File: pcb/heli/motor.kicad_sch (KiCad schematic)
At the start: 6 parts

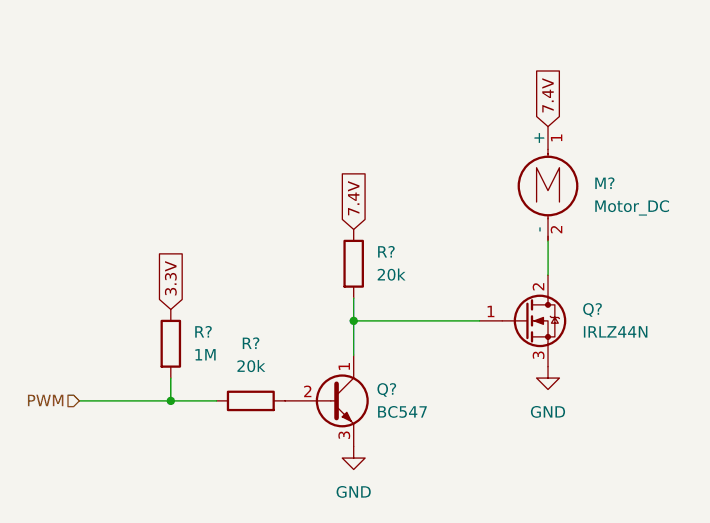
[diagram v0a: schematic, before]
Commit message: 
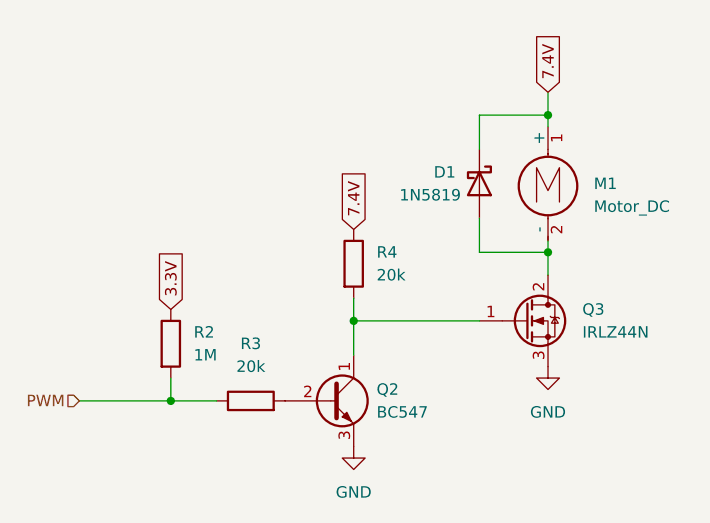
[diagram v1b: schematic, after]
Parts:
- added D1: 1N5819, Diode_THT:D_DO-41_SOD81_P10.16mm_Horizontal, symbol Diode:1N5819
- gave numbers to parts that had none: 6
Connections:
- net 7.4V: now also D1.1 (K)
- net at M1.2 (-), Q3.2 (D): now also D1.2 (A)
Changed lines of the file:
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@@
   (junction (at 54.61 59.69) (diameter 0) (color 0 0 0 0)
   )
+  (junction (at 76.2 36.83) (diameter 0) (color 0 0 0 0)
+  )
+  (junction (at 76.2 52.07) (diameter 0) (color 0 0 0 0)
+  )
   (junction (at 34.29 68.58) (diameter 0) (color 0 0 0 0)
   )
+  (wire (pts (xy 76.2 52.07) (xy 76.2 54.61))
+    (stroke (width 0) (type default) (color 0 0 0 0))
+  )
+  (wire (pts (xy 68.58 36.83) (xy 76.2 36.83))
+    (stroke (width 0) (type default) (color 0 0 0 0))
+  )
+  (wire (pts (xy 68.58 52.07) (xy 76.2 52.07))
+    (stroke (width 0) (type default) (color 0 0 0 0))
+  )
   (wire (pts (xy 54.61 59.69) (xy 54.61 57.15))
     (stroke (width 0) (type default) (color 0 0 0 0))
   )
-  (wire (pts (xy 76.2 50.8) (xy 76.2 54.61))
+  (wire (pts (xy 76.2 50.8) (xy 76.2 52.07))
+    (stroke (width 0) (type default) (color 0 0 0 0))
+  )
+  (wire (pts (xy 68.58 40.64) (xy 68.58 36.83))
+    (stroke (width 0) (type default) (color 0 0 0 0))
+  )
+  (wire (pts (xy 76.2 36.83) (xy 76.2 38.1))
     (stroke (width 0) (type default) (color 0 0 0 0))
   )
@@
   )
   (wire (pts (xy 34.29 68.58) (xy 39.37 68.58))
+    (stroke (width 0) (type default) (color 0 0 0 0))
+  )
+  (wire (pts (xy 76.2 34.29) (xy 76.2 36.83))
+    (stroke (width 0) (type default) (color 0 0 0 0))
+  )
+  (wire (pts (xy 68.58 48.26) (xy 68.58 52.07))
     (stroke (width 0) (type default) (color 0 0 0 0))
   )
@@
     )
   )
-  (global_label "7.4V" (shape input) (at 76.2 38.1 90) (fields_autoplaced)
+  (global_label "7.4V" (shape input) (at 76.2 34.29 90) (fields_autoplaced)
     (effects (font (size 1.27 1.27)) (justify left))
-    (property "Intersheet References" "${INTERSHEET_REFS}" (id 0) (at 76.1206 31.5745 90)
+    (property "Intersheet References" "${INTERSHEET_REFS}" (id 0) (at 76.1206 27.7645 90)
       (effects (font (size 1.27 1.27)) (justify left) hide)
     )
@@
   (symbol (lib_id "power:GND") (at 54.61 73.66 0) (unit 1)
     (in_bom yes) (on_board yes) (fields_autoplaced)
-    (property "Reference" "#PWR?" (id 0) (at 54.61 80.01 0)
+    (property "Reference" "#PWR0115" (id 0) (at 54.61 80.01 0)
       (effects (font (size 1.27 1.27)) hide)
     )
@@
   (symbol (lib_id "Device:R") (at 34.29 62.23 0) (unit 1)
     (in_bom yes) (on_board yes) (fields_autoplaced)
-    (property "Reference" "R?" (id 0) (at 36.83 60.9599 0)
+    (property "Reference" "R2" (id 0) (at 36.83 60.9599 0)
       (effects (font (size 1.27 1.27)) (justify left))
     )
@@
     (pin "2")
   )
+  (symbol (lib_id "Diode:1N5819") (at 68.58 44.45 270) (unit 1)
+    (in_bom yes) (on_board yes)
+    (property "Reference" "D1" (id 0) (at 63.5 43.18 90)
+      (effects (font (size 1.27 1.27)) (justify left))
+    )
+    (property "Value" "1N5819" (id 1) (at 59.69 45.72 90)
+      (effects (font (size 1.27 1.27)) (justify left))
+    )
+    (property "Footprint" "Diode_THT:D_DO-41_SOD81_P10.16mm_Horizontal" (id 2) (at 64.135 44.45 0)
+      (effects (font (size 1.27 1.27)) hide)
+    )
+    (property "Datasheet" "http://www.vishay.com/docs/88525/1n5817.pdf" (id 3) (at 68.58 44.45 0)
+      (effects (font (size 1.27 1.27)) hide)
+    )
+    (pin "1")
+    (pin "2")
+  )
   (symbol (lib_id "Device:R") (at 43.18 68.58 90) (unit 1)
     (in_bom yes) (on_board yes) (fields_autoplaced)
-    (property "Reference" "R?" (id 0) (at 43.18 62.23 90))
+    (property "Reference" "R3" (id 0) (at 43.18 62.23 90))
     (property "Value" "20k" (id 1) (at 43.18 64.77 90))
     (property "Footprint" "" (id 2) (at 43.18 70.358 90)
@@
   (symbol (lib_id "Transistor_BJT:BC547") (at 52.07 68.58 0) (unit 1)
     (in_bom yes) (on_board yes) (fields_autoplaced)
-    (property "Reference" "Q?" (id 0) (at 57.15 67.3099 0)
+    (property "Reference" "Q2" (id 0) (at 57.15 67.3099 0)
       (effects (font (size 1.27 1.27)) (justify left))
     )
@@
   (symbol (lib_id "power:GND") (at 76.2 64.77 0) (unit 1)
     (in_bom yes) (on_board yes) (fields_autoplaced)
-    (property "Reference" "#PWR?" (id 0) (at 76.2 71.12 0)
+    (property "Reference" "#PWR0114" (id 0) (at 76.2 71.12 0)
       (effects (font (size 1.27 1.27)) hide)
     )
@@
   (symbol (lib_id "Device:R") (at 54.61 53.34 0) (unit 1)
     (in_bom yes) (on_board yes) (fields_autoplaced)
-    (property "Reference" "R?" (id 0) (at 57.15 52.0699 0)
+    (property "Reference" "R4" (id 0) (at 57.15 52.0699 0)
       (effects (font (size 1.27 1.27)) (justify left))
     )
@@
   (symbol (lib_id "Transistor_FET:IRLZ44N") (at 73.66 59.69 0) (unit 1)
     (in_bom yes) (on_board yes) (fields_autoplaced)
-    (property "Reference" "Q?" (id 0) (at 80.01 58.4199 0)
+    (property "Reference" "Q3" (id 0) (at 80.01 58.4199 0)
       (effects (font (size 1.27 1.27)) (justify left))
     )
@@
   (symbol (lib_id "Motor:Motor_DC") (at 76.2 43.18 0) (unit 1)
     (in_bom yes) (on_board yes) (fields_autoplaced)
-    (property "Reference" "M?" (id 0) (at 81.28 44.4499 0)
-      (effects (font (size 1.27 1.27)) (justify left))
-    )
+    (property "Reference" "M1" (id 0) (at 81.28 44.4499 0)
+      (effects (font (size 1.27 1.27)) (justify left))
+    )

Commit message: 
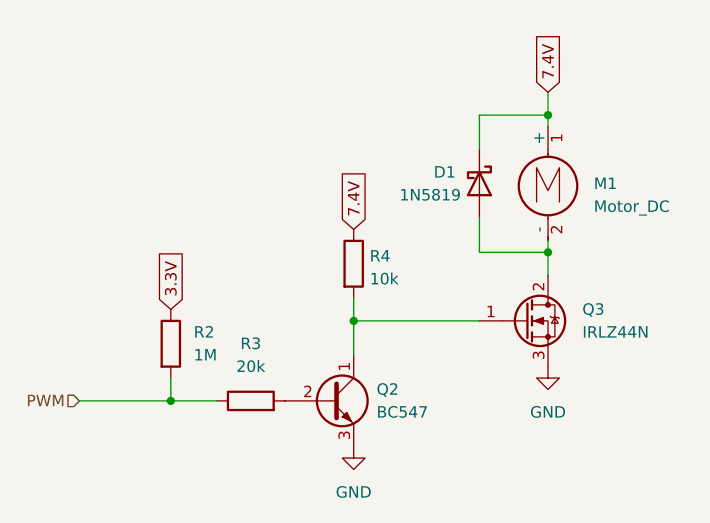
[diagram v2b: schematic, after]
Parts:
- R4: value 20k -> 10k
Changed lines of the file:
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@@
   (symbol (lib_id "Device:R") (at 54.61 53.34 0) (unit 1)
     (in_bom yes) (on_board yes) (fields_autoplaced)
-    (property "Reference" "R4" (id 0) (at 57.15 52.0699 0)
+    (property "Reference" "R4" (id 0) (at 56.388 52.5053 0)
       (effects (font (size 1.27 1.27)) (justify left))
     )
-    (property "Value" "20k" (id 1) (at 57.15 54.6099 0)
+    (property "Value" "10k" (id 1) (at 56.388 55.0422 0)
       (effects (font (size 1.27 1.27)) (justify left))
     )

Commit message: 
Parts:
- M1: footprint (none) -> Connector_PinHeader_2.54mm:PinHeader_1x02_P2.54mm_Vertical
- R2, R3, R4: footprint (none) -> Resistor_SMD:R_0603_1608Metric
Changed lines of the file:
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@@
       (effects (font (size 1.27 1.27)) (justify left))
     )
-    (property "Footprint" "" (id 2) (at 32.512 62.23 90)
+    (property "Footprint" "Resistor_SMD:R_0603_1608Metric" (id 2) (at 32.512 62.23 90)
       (effects (font (size 1.27 1.27)) hide)
     )
@@
     (property "Reference" "R3" (id 0) (at 43.18 62.23 90))
     (property "Value" "20k" (id 1) (at 43.18 64.77 90))
-    (property "Footprint" "" (id 2) (at 43.18 70.358 90)
+    (property "Footprint" "Resistor_SMD:R_0603_1608Metric" (id 2) (at 43.18 70.358 90)
       (effects (font (size 1.27 1.27)) hide)
     )
@@
       (effects (font (size 1.27 1.27)) (justify left))
     )
-    (property "Footprint" "" (id 2) (at 52.832 53.34 90)
+    (property "Footprint" "Resistor_SMD:R_0603_1608Metric" (id 2) (at 52.832 53.34 90)
       (effects (font (size 1.27 1.27)) hide)
     )
@@
       (effects (font (size 1.27 1.27)) (justify left))
     )
-    (property "Footprint" "" (id 2) (at 76.2 45.466 0)
+    (property "Footprint" "Connector_PinHeader_2.54mm:PinHeader_1x02_P2.54mm_Vertical" (id 2) (at 76.2 45.466 0)
       (effects (font (size 1.27 1.27)) hide)
     )

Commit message: 
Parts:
- renumbered D1 to D2, R4 to R10, R2 to R8, R3 to R9
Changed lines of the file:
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@@
   (symbol (lib_id "power:GND") (at 54.61 73.66 0) (unit 1)
     (in_bom yes) (on_board yes) (fields_autoplaced)
-    (property "Reference" "#PWR0115" (id 0) (at 54.61 80.01 0)
+    (property "Reference" "#PWR027" (id 0) (at 54.61 80.01 0)
       (effects (font (size 1.27 1.27)) hide)
     )
@@
   (symbol (lib_id "Device:R") (at 34.29 62.23 0) (unit 1)
     (in_bom yes) (on_board yes) (fields_autoplaced)
-    (property "Reference" "R2" (id 0) (at 36.83 60.9599 0)
+    (property "Reference" "R8" (id 0) (at 36.83 60.9599 0)
       (effects (font (size 1.27 1.27)) (justify left))
     )
@@
   (symbol (lib_id "Diode:1N5819") (at 68.58 44.45 270) (unit 1)
     (in_bom yes) (on_board yes)
-    (property "Reference" "D1" (id 0) (at 63.5 43.18 90)
+    (property "Reference" "D2" (id 0) (at 63.5 43.18 90)
       (effects (font (size 1.27 1.27)) (justify left))
     )
@@
   (symbol (lib_id "Device:R") (at 43.18 68.58 90) (unit 1)
     (in_bom yes) (on_board yes) (fields_autoplaced)
-    (property "Reference" "R3" (id 0) (at 43.18 62.23 90))
+    (property "Reference" "R9" (id 0) (at 43.18 62.23 90))
     (property "Value" "20k" (id 1) (at 43.18 64.77 90))
     (property "Footprint" "Resistor_SMD:R_0603_1608Metric" (id 2) (at 43.18 70.358 90)
@@
   (symbol (lib_id "power:GND") (at 76.2 64.77 0) (unit 1)
     (in_bom yes) (on_board yes) (fields_autoplaced)
-    (property "Reference" "#PWR0114" (id 0) (at 76.2 71.12 0)
+    (property "Reference" "#PWR028" (id 0) (at 76.2 71.12 0)
       (effects (font (size 1.27 1.27)) hide)
     )
@@
   (symbol (lib_id "Device:R") (at 54.61 53.34 0) (unit 1)
     (in_bom yes) (on_board yes) (fields_autoplaced)
-    (property "Reference" "R4" (id 0) (at 56.388 52.5053 0)
+    (property "Reference" "R10" (id 0) (at 56.388 52.5053 0)
       (effects (font (size 1.27 1.27)) (justify left))
     )

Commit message: 
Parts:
- D2: footprint Diode_THT:D_DO-41_SOD81_P10.16mm_Horizontal -> Diode_SMD:D_SOD-123F; DIGIKEY (none) -> https://www.digikey.de/en/products/detail/smc-diode-solutio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
- M1: DIGIKEY (none) -> https://www.digikey.de/en/products/detail/adam-tech/PH1-10-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
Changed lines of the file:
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@@
       (effects (font (size 1.27 1.27)) (justify left))
     )
-    (property "Footprint" "Diode_THT:D_DO-41_SOD81_P10.16mm_Horizontal" (id 2) (at 64.135 44.45 0)
+    (property "Footprint" "Diode_SMD:D_SOD-123F" (id 2) (at 64.135 44.45 0)
       (effects (font (size 1.27 1.27)) hide)
     )
     (property "Datasheet" "http://www.vishay.com/docs/88525/1n5817.pdf" (id 3) (at 68.58 44.45 0)
+      (effects (font (size 1.27 1.27)) hide)
+    )
+    (property "DIGIKEY" "https://www.digikey.de/en/products/detail/smc-diode-solutions/1N5819W/15964237" (id 4) (at 68.58 44.45 0)
       (effects (font (size 1.27 1.27)) hide)
     )
@@
       (effects (font (size 1.27 1.27)) hide)
     )
+    (property "DIGIKEY" "https://www.digikey.de/en/products/detail/adam-tech/PH1-10-UA/9830653" (id 4) (at 76.2 43.18 0)
+      (effects (font (size 1.27 1.27)) hide)
+    )

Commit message: 
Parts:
- R8: DIGIKEY (none) -> https://www.digikey.de/en/products/detail/walsin-technology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
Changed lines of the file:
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@@
+      (effects (font (size 1.27 1.27)) hide)
+    )
+    (property "DIGIKEY" "https://www.digikey.de/en/products/detail/walsin-technology-corporation/WR06X1004FTL/13241115" (id 4) (at 34.29 62.23 0)
       (effects (font (size 1.27 1.27)) hide)
     )

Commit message: 
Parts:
- R8: DIGIKEY https://www.digikey.de/en/products/detail/walsin-technology-corporation/WR06X1004FTL/13241115 -> https://www.digikey.de/en/products/detail/walsin-technology-corporation/WR06X105-JTL/13239221
- R9: DIGIKEY (none) -> https://www.digikey.de/en/products/detail/stackpole-electro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
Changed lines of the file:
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@@
       (effects (font (size 1.27 1.27)) hide)
     )
-    (property "DIGIKEY" "https://www.digikey.de/en/products/detail/walsin-technology-corporation/WR06X1004FTL/13241115" (id 4) (at 34.29 62.23 0)
+    (property "DIGIKEY" "https://www.digikey.de/en/products/detail/walsin-technology-corporation/WR06X105-JTL/13239221" (id 4) (at 34.29 62.23 0)
       (effects (font (size 1.27 1.27)) hide)
     )
@@
       (effects (font (size 1.27 1.27)) hide)
     )
+    (property "DIGIKEY" "https://www.digikey.de/en/products/detail/stackpole-electronics-inc/RMCF0603JT20K0/1758001" (id 4) (at 43.18 68.58 0)
+      (effects (font (size 1.27 1.27)) hide)
+    )

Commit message: 
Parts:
- Q2, Q3: DIGIKEY (none) -> -
- R10: DIGIKEY (none) -> https://www.digikey.de/en/products/detail/walsin-technology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
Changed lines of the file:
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@@
       (effects (font (size 1.27 1.27)) (justify left) hide)
+    )
+    (property "DIGIKEY" "-" (id 4) (at 52.07 68.58 0)
+      (effects (font (size 1.27 1.27)) hide)
     )
     (pin "1")
@@
       (effects (font (size 1.27 1.27)) hide)
     )
+    (property "DIGIKEY" "https://www.digikey.de/en/products/detail/walsin-technology-corporation/WR06X103-JTL/13239132" (id 4) (at 54.61 53.34 0)
+      (effects (font (size 1.27 1.27)) hide)
+    )
     (pin "1")
     (pin "2")
@@
       (effects (font (size 1.27 1.27)) (justify left) hide)
     )
+    (property "DIGIKEY" "-" (id 4) (at 73.66 59.69 0)
+      (effects (font (size 1.27 1.27)) hide)
+    )
     (pin "1")
